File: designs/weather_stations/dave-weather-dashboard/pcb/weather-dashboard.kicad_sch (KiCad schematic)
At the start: 6 parts, among them SW2 SW_Omron_B3FS, U1 WEMOS_S2_Mini, U4 TFT_ST7735_SD

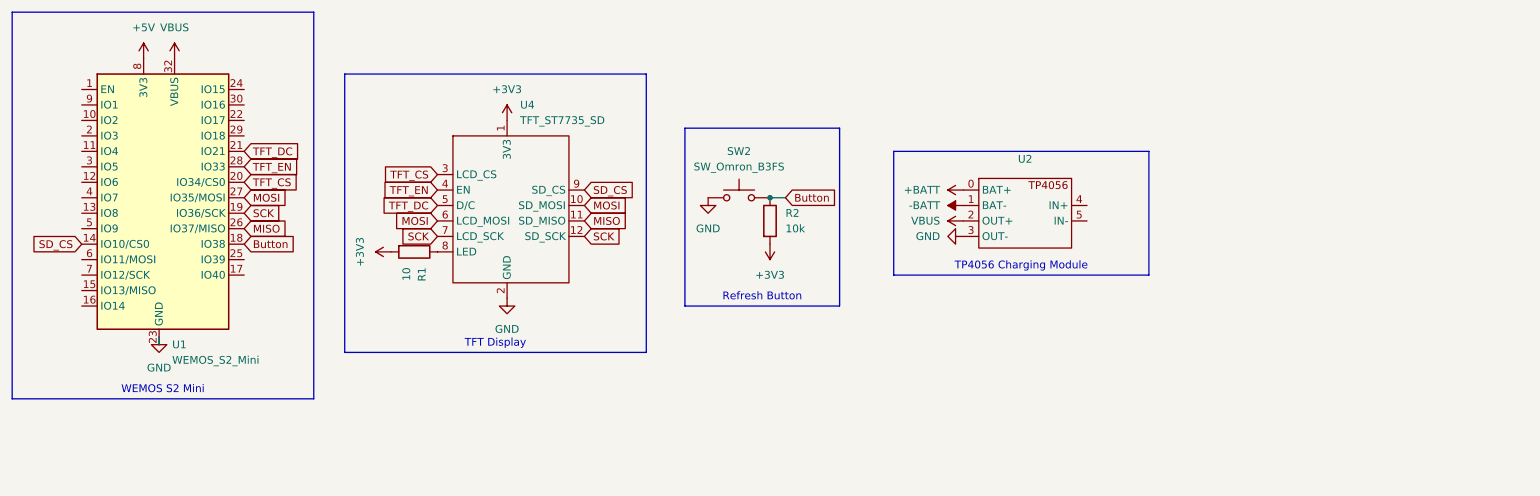
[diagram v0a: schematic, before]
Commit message: Removed external resistor to use internal resistor and added load sharing circuit along with updated casing
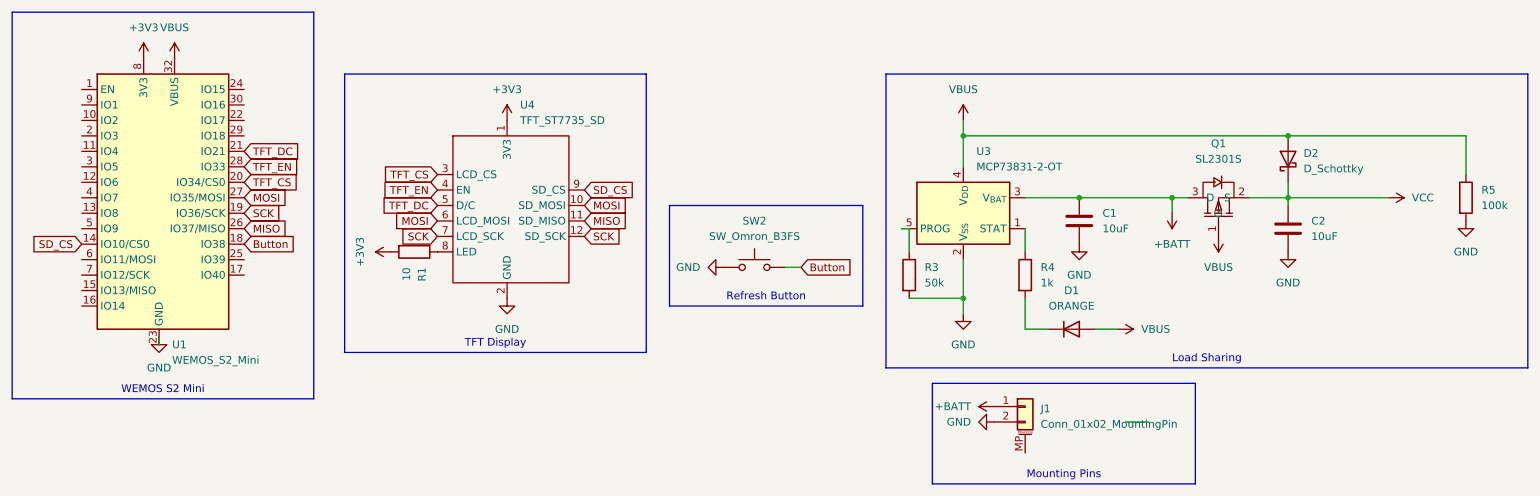
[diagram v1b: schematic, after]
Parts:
- removed R2: 10k, Resistor_THT:R_Axial_DIN0309_L9.0mm_D3.2mm_P12.70mm_Horizontal, symbol Device:R
- removed U2: ~, asylum-weather:TP4056, symbol asylum-weather:TP4056
- added C1, C2: 10uF, Capacitor_SMD:C_1206_3216Metric, symbol Device:C
- added D1: ORANGE, LED_SMD:LED_1206_3216Metric_ReverseMount_Hole1.8x2.4mm, symbol Device:D
- added D2: D_Schottky, kicad-libraries:DO-214AC, symbol Device:D_Schottky
- added J1: Conn_01x02_MountingPin, Connector_PinHeader_1.00mm:PinHeader_1x02_P1.00mm_Vertical, symbol Connector_Generic_MountingPin:Conn_01x02_MountingPin
- added Q1: SL2301S, Package_TO_SOT_SMD:SOT-23, symbol sl2301s:SL2301S
- added R3: 50k, Resistor_SMD:R_1206_3216Metric, symbol Device:R
- added R4: 1k, Resistor_SMD:R_1206_3216Metric, symbol Device:R
- added R5: 100k, Resistor_SMD:R_1206_3216Metric, symbol Device:R
- added U3: MCP73831-2-OT, Package_TO_SOT_SMD:SOT-23-5, symbol Battery_Management:MCP73831-2-OT
- R1: footprint Resistor_THT:R_Axial_DIN0309_L9.0mm_D3.2mm_P12.70mm_Horizontal -> Resistor_SMD:R_1206_3216Metric
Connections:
- net +5V is gone; now on net +3V3: U1.8 (3V3)
- net +BATT: now also C1.1, J1.1 (Pin_1), Q1.3 (D), U3.3 (V_{BAT})
- net GND: now also C1.2, C2.2, J1.2 (Pin_2), R3.2, R5.2, U3.2 (V_{SS})
- net VBUS: now also D1.2 (A), D2.2 (A), Q1.1 (G), R5.1, U3.4 (V_{DD})
- new net: R4.1, U3.1 (STAT)
- new net: R3.1, U3.5 (PROG)
- new net: D1.1 (K), R4.2
- new net VCC: C2.1, D2.1 (K), Q1.2 (S)
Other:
- moved on the sheet: SW2

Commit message: screenshots
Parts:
- removed Q1: SL2301S, Package_TO_SOT_SMD:SOT-23, symbol sl2301s:SL2301S
- added Q2: AO3401A, Package_TO_SOT_SMD:SOT-23, symbol Transistor_FET:AO3401A
- C1, C2: footprint Capacitor_SMD:C_1206_3216Metric -> Capacitor_SMD:C_0603_1608Metric
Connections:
- net +BATT: now also Q2.3 (D)
- net VCC: now also Q2.2 (S)
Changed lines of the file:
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@@
 			)
 		)
-		(property "Footprint" "Capacitor_SMD:C_1206_3216Metric"
+		(property "Footprint" "Capacitor_SMD:C_0603_1608Metric"
 			(at 229.5652 57.15 0)
 			(effects
@@
 	)
 	(symbol
+		(lib_id "Transistor_FET:AO3401A")
+		(at 217.17 50.8 90)
+		(unit 1)
+		(exclude_from_sim no)
+		(in_bom yes)
+		(on_board yes)
+		(dnp no)
+		(fields_autoplaced yes)
+		(property "Reference" "Q2"
+			(at 217.17 41.91 90)
+			(effects
+				(font
+					(size 1.27 1.27)
+				)
+			)
+		)
+		(property "Value" "AO3401A"
+			(at 217.17 44.45 90)
+			(effects
+				(font
+					(size 1.27 1.27)
+				)
+			)
+		)
+		(property "Footprint" "Package_TO_SOT_SMD:SOT-23"
+			(at 219.075 45.72 0)
+			(effects
+				(font
+					(size 1.27 1.27)
+					(italic yes)
+				)
+				(justify left)
+				(hide yes)
+			)
+		)
+		(property "Datasheet" "http://www.aosmd.com/pdfs/datasheet/AO3401A.pdf"
+			(at 220.98 45.72 0)
+			(effects
+				(font
+					(size 1.27 1.27)
+				)
+				(justify left)
+				(hide yes)
+			)
+		)
+		(property "Description" "-4.0A Id, -30V Vds, P-Channel MOSFET, SOT-23"
+			(at 217.17 50.8 0)
+			(effects
+				(font
+					(size 1.27 1.27)
+				)
+				(hide yes)
+			)
+		)
+		(pin "2"
+		)
+		(pin "3"
+		)
+		(pin "1"
+		)
+		(instances
+			(project ""
+				(path "/c79e4914-4b7d-4f53-856d-980a3bf819a4"
+					(reference "Q2")
+					(unit 1)
+				)
+			)
+		)
+	)
+	(symbol
 		(lib_id "power:+BATT")
 		(at 180.34 82.55 90)
@@
 			)
 		)
-		(property "Footprint" "Capacitor_SMD:C_1206_3216Metric"
+		(property "Footprint" "Capacitor_SMD:C_0603_1608Metric"
 			(at 195.2752 55.88 0)
 			(effects
@@
 					(unit 1)
 				)
-			)
-		)
-	)
-	(symbol
-		(lib_id "sl2301s:SL2301S")
-		(at 217.17 50.8 90)
-		(unit 1)
-		(exclude_from_sim no)
-		(in_bom yes)
-		(on_board yes)
-		(dnp no)
-		(fields_autoplaced yes)
-		(property "Reference" "Q1"
-			(at 217.17 39.37 90)
-			(effects
-				(font
-					(size 1.27 1.27)
-				)
-			)
-		)
-		(property "Value" "SL2301S"
-			(at 217.17 41.91 90)
-			(effects
-				(font
-					(size 1.27 1.27)
-				)
-			)
-		)
-		(property "Footprint" "Package_TO_SOT_SMD:SOT-23"
-			(at 229.87 50.8 0)
-			(effects
-				(font
-					(size 1.27 1.27)
-				)
-				(hide yes)
-			)
-		)
-		(property "Datasheet" ""
-			(at 217.17 50.8 0)
-			(effects
-				(font
-					(size 1.27 1.27)
-				)
-				(hide yes)
-			)
-		)
-		(property "Description" ""
-			(at 217.17 50.8 0)
-			(effects
-				(font
-					(size 1.27 1.27)
-				)
-				(hide yes)
-			)
-		)
-		(property "LCSC Part" "C473810"
-			(at 232.41 50.8 0)
-			(effects
-				(font
-					(size 1.27 1.27)
-				)
-				(hide yes)
-			)
-		)
-		(pin "2"
-		)
-		(pin "3"
-		)
-		(pin "1"
-		)
-		(instances
-			(project ""
-				(path "/c79e4914-4b7d-4f53-856d-980a3bf819a4"
-					(reference "Q1")
-					(unit 1)
-				)
